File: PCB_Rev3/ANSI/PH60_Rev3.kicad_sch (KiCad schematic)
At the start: 45 parts, among them J1 USB_C_Receptacle_USB2.0_16P, J2 Conn_01x02, J3 Conn_01x02_Pin, J4 Conn_01x02_Pin, SW1 SW_SPDT_321, U1 TLV62569DBV, U2 RP2040, U4 ETA6093, U6 W25Q16JVSS, Y1 Crystal_GND24

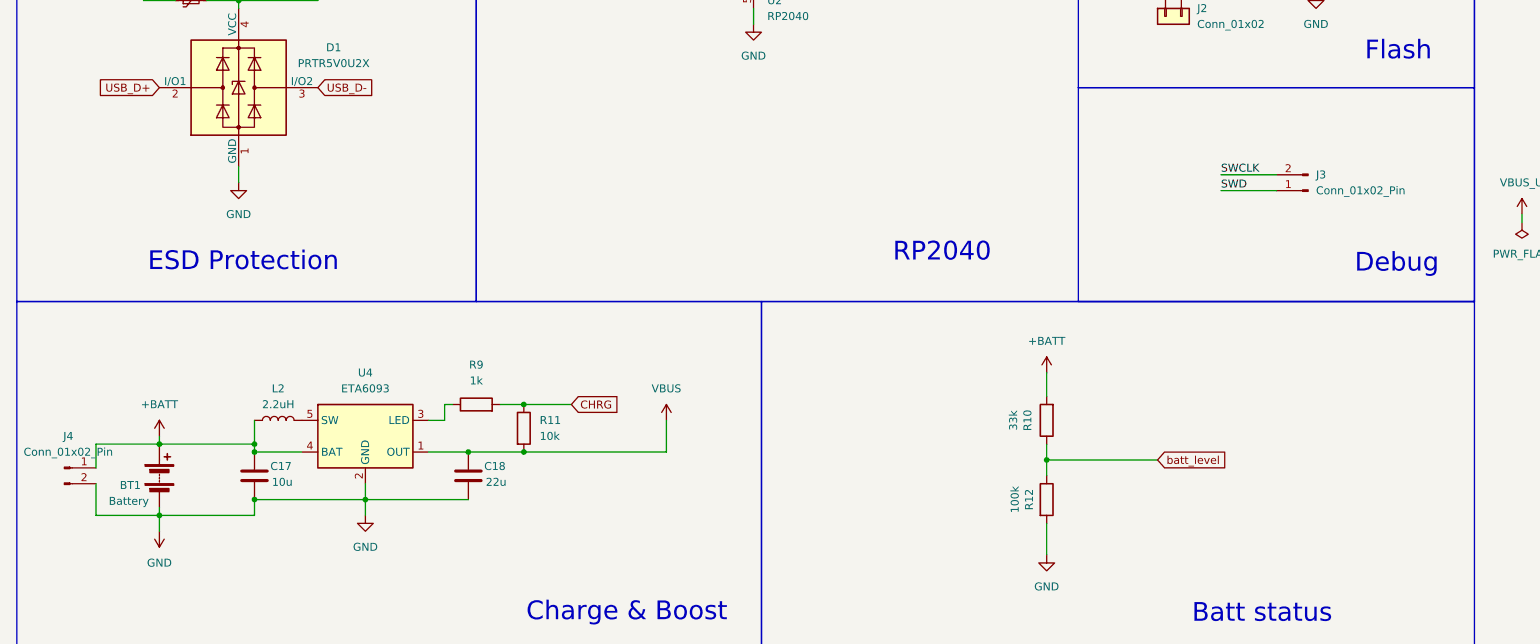
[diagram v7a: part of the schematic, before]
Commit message: Add mounting hole
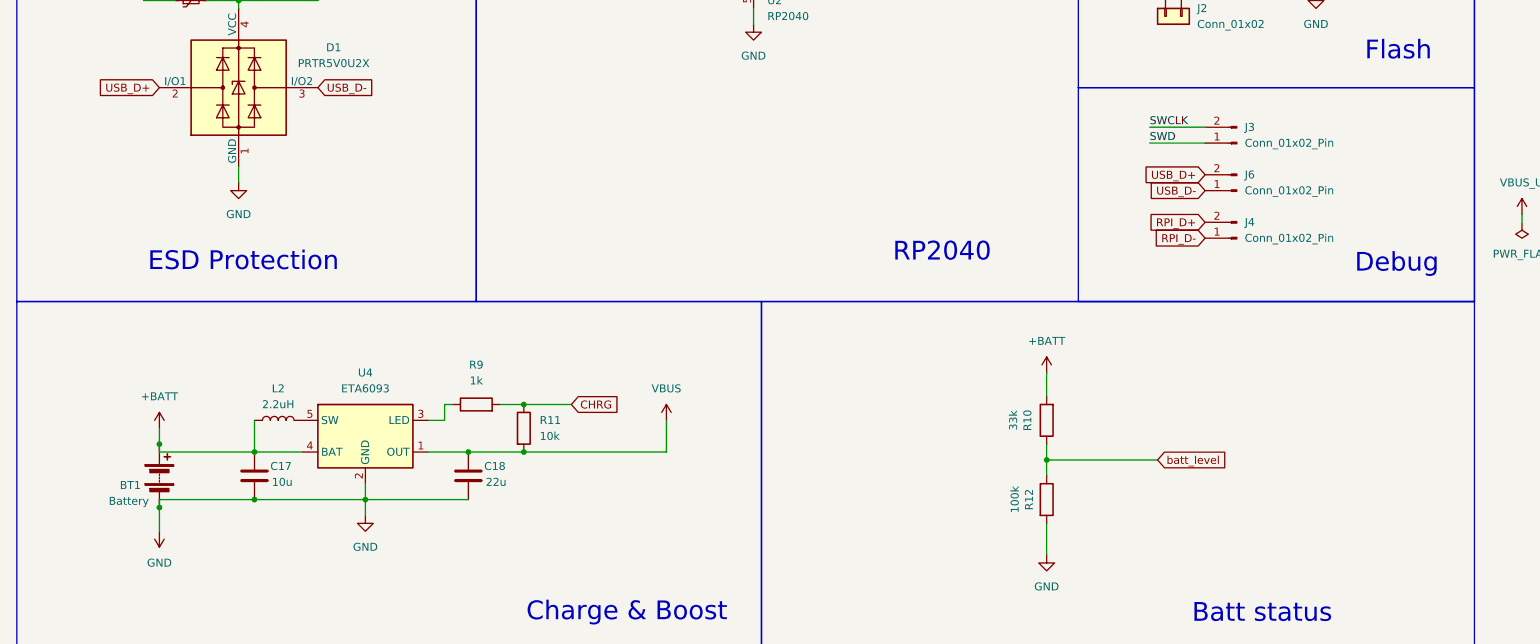
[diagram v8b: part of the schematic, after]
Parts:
- added J6: Conn_01x02_Pin, Connector_PinHeader_2.00mm:PinHeader_1x02_P2.00mm_Vertical, symbol Connector:Conn_01x02_Pin
- BT1: footprint Connector_Molex:Molex_PicoBlade_53261-0271_1x02-1MP_P1.25mm_Horizontal -> PH60:Molex_PicoBlade_With_Via
- J3: footprint (none) -> Connector_PinHeader_2.00mm:PinHeader_1x02_P2.00mm_Vertical
- J4: footprint Connector_PinHeader_1.27mm:PinHeader_1x02_P1.27mm_Vertical -> Connector_PinHeader_2.00mm:PinHeader_1x02_P2.00mm_Vertical
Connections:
- net +BATT: no longer J4.1 (Pin_1)
- net GND: no longer J4.2 (Pin_2)
- net RPI_D+: now also J4.2 (Pin_2)
- net RPI_D-: now also J4.1 (Pin_1)
- net USB_D+: now also J6.2 (Pin_2)
- net USB_D-: now also J6.1 (Pin_1)
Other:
- moved on the sheet: J3
